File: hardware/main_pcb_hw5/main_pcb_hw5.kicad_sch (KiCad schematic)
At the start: 24 parts, among them J1 MEGA TOP, J10 GBA_Slot, J2 MEGA BOTTOM, J3 CART SLOT TOP ROW, J4 CART SLOT BOTTOM ROW, J5 MEGA SIDE, J6 5V USB, J7 Conn_01x07, J8 EXP2, J9 EXP1, M2_1 Screw_Terminal_01x01, M2_2 Screw_Terminal_01x01, M2_3 Screw_Terminal_01x01, M2_4 Screw_Terminal_01x01, M2_5 Screw_Terminal_01x01, M2_6 Screw_Terminal_01x01, M2_7 Screw_Terminal_01x01, M2_8 Screw_Terminal_01x01, M2_9 Screw_Terminal_01x01, SW1 VOLTAGE SWITCH, SW2 POWER SWITCH

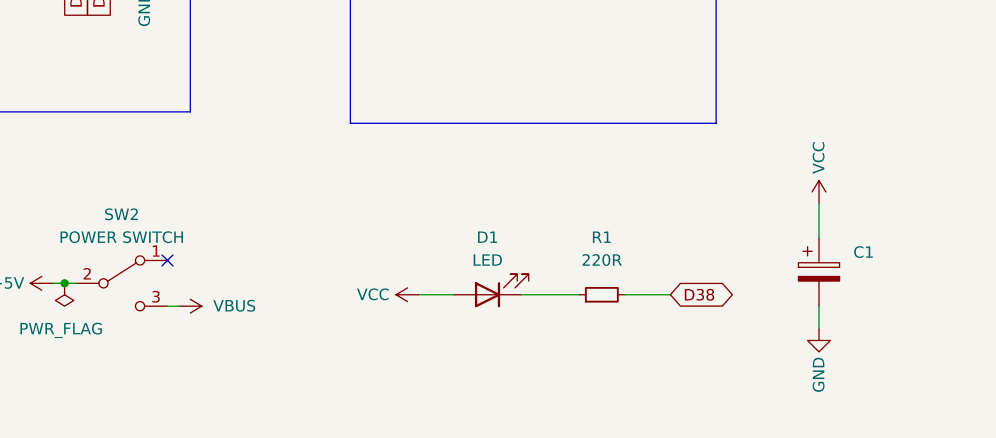
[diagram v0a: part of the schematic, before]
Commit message: Move switches to right side
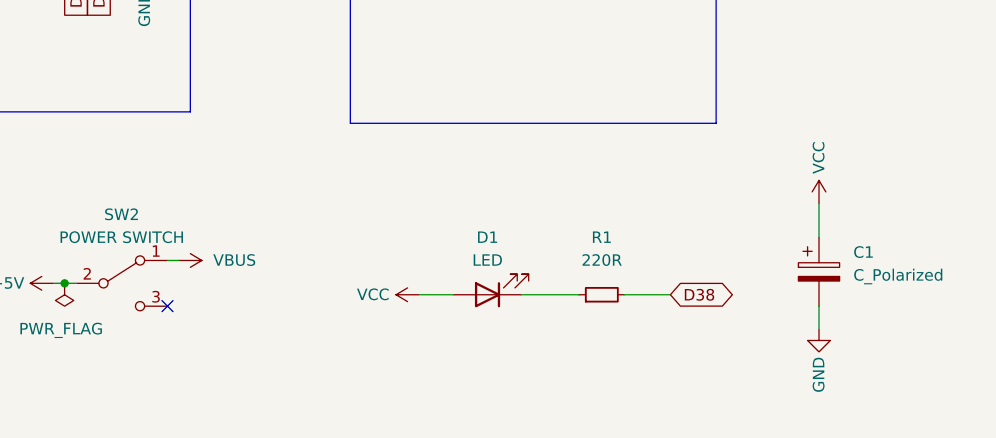
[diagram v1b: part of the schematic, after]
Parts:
- C1: value (none) -> C_Polarized
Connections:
- net VBUS: now also SW2.1 (A); no longer SW2.3 (C)
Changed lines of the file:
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@@
   (title_block
     (title "OSCR HW5")
-    (date "2022-05-16")
-    (rev "V1")
+    (date "2022-06-04")
+    (rev "V2")
   )
   (junction (at 248.92 45.72) (diameter 0) (color 0 0 0 0)
@@
   (no_connect (at 194.31 113.03))
   (no_connect (at 36.83 30.48))
-  (no_connect (at 199.39 149.86))
+  (no_connect (at 199.39 154.94))
   (no_connect (at 39.37 30.48))
   (no_connect (at 35.56 96.52))
@@
     (stroke (width 0) (type default) (color 0 0 0 0))
   )
-  (wire (pts (xy 199.39 154.94) (xy 200.66 154.94))
+  (wire (pts (xy 199.39 149.86) (xy 200.66 149.86))
     (stroke (width 0) (type default) (color 0 0 0 0))
   )
@@
     (pin "9")
   )
-  (symbol (lib_id "power:VBUS") (at 200.66 154.94 270) (unit 1)
+  (symbol (lib_id "power:VBUS") (at 200.66 149.86 270) (unit 1)
     (in_bom yes) (on_board yes) (fields_autoplaced)
-    (property "Reference" "#PWR0103" (id 0) (at 196.85 154.94 0)
-      (effects (font (size 1.27 1.27)) hide)
-    )
-    (property "Value" "VBUS" (id 1) (at 204.47 154.9399 90)
+    (property "Reference" "#PWR0103" (id 0) (at 196.85 149.86 0)
+      (effects (font (size 1.27 1.27)) hide)
+    )
+    (property "Value" "VBUS" (id 1) (at 204.47 149.8599 90)
       (effects (font (size 1.27 1.27)) (justify left))
     )
-    (property "Footprint" "" (id 2) (at 200.66 154.94 0)
-      (effects (font (size 1.27 1.27)) hide)
-    )
-    (property "Datasheet" "" (id 3) (at 200.66 154.94 0)
+    (property "Footprint" "" (id 2) (at 200.66 149.86 0)
+      (effects (font (size 1.27 1.27)) hide)
+    )
+    (property "Datasheet" "" (id 3) (at 200.66 149.86 0)
       (effects (font (size 1.27 1.27)) hide)
     )
@@
       (effects (font (size 1.27 1.27)) (justify left))
     )
-    (property "Value" "" (id 1) (at 275.59 151.5109 0)
+    (property "Value" "C_Polarized" (id 1) (at 275.59 151.5109 0)
       (effects (font (size 1.27 1.27)) (justify left))
     )

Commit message: Add HW5 Rev. 3
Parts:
- added JP1: Arduino powered by VCC, symbol Jumper:SolderJumper_2_Open
- added JP2: Arduino powered by 5V, symbol Jumper:SolderJumper_2_Open
- added JP3: (no value), symbol Jumper:SolderJumper_2_Open
- SW1: value VOLTAGE SWITCH -> (none)
- SW2: value POWER SWITCH -> (none)
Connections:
- net +3V3: now also JP3.2 (B)
- net +5V: now also JP2.1 (A)
- net VCC: now also JP1.1 (A); no longer J1.37 (Pin_37), J1.38 (Pin_38)
- net +3.3VA: now reaches J1.35 (Pin_35)
- net +3.3VA: now also J1.36 (Pin_36), JP3.1 (A)
- new net VDDA: J1.37 (Pin_37), J1.38 (Pin_38), JP1.2 (B), JP2.2 (B)
- no-connect marks 12 -> 10

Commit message: Update silkscreen
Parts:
- JP1: value Arduino powered by VCC -> (none)
- JP2: value Arduino powered by 5V -> (none)
- SW1: value (none) -> VOLTAGE
- SW2: value (none) -> POWER
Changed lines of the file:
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@@
     (in_bom yes) (on_board yes) (fields_autoplaced)
     (property "Reference" "JP2" (id 0) (at 31.75 182.88 0))
-    (property "Value" "Arduino powered by 5V" (id 1) (at 31.75 185.42 0))
+    (property "Value" "" (id 1) (at 31.75 185.42 0))
     (property "Footprint" "" (id 2) (at 31.75 189.23 0)
       (effects (font (size 1.27 1.27)) hide)
@@
     (in_bom yes) (on_board yes) (fields_autoplaced)
     (property "Reference" "JP1" (id 0) (at 31.75 171.45 0))
-    (property "Value" "Arduino powered by VCC" (id 1) (at 31.75 173.99 0))
+    (property "Value" "" (id 1) (at 31.75 173.99 0))
     (property "Footprint" "" (id 2) (at 31.75 177.8 0)
       (effects (font (size 1.27 1.27)) hide)
@@
     (in_bom yes) (on_board yes) (fields_autoplaced)
     (property "Reference" "SW2" (id 0) (at 194.31 144.78 0))
-    (property "Value" "" (id 1) (at 194.31 147.32 0))
+    (property "Value" "POWER" (id 1) (at 194.31 147.32 0))
     (property "Footprint" "" (id 2) (at 194.31 152.4 0)
       (effects (font (size 1.27 1.27)) hide)
@@
       (effects (font (size 1.27 1.27)) hide)
     )
-    (property "Value" "" (id 1) (at 43.18 86.36 90))
+    (property "Value" "+3.3VA" (id 1) (at 43.18 86.36 90))
     (property "Footprint" "" (id 2) (at 43.18 92.71 0)
       (effects (font (size 1.27 1.27)) hide)
@@
     (in_bom yes) (on_board yes) (fields_autoplaced)
     (property "Reference" "SW1" (id 0) (at 161.29 144.78 0))
-    (property "Value" "" (id 1) (at 161.29 147.32 0))
+    (property "Value" "VOLTAGE" (id 1) (at 161.29 147.32 0))
     (property "Footprint" "" (id 2) (at 161.29 152.4 0)
       (effects (font (size 1.27 1.27)) hide)
@@
     )
     (path "/9b821643-0a09-4ed0-af40-76467a90d5d5"
-      (reference "JP1") (unit 1) (value "Arduino powered by VCC") (footprint "")
+      (reference "JP1") (unit 1) (value "J1") (footprint "")
     )
     (path "/5b67058f-fbd0-4ef7-ae7b-c94a6074918c"
-      (reference "JP2") (unit 1) (value "Arduino powered by 5V") (footprint "")
+      (reference "JP2") (unit 1) (value "Testpoints 1 2") (footprint "")
     )
     (path "/370f34de-8b3d-462d-a13b-4bf97a89f644"
-      (reference "JP3") (unit 1) (value "3V3 from Arduino") (footprint "")
+      (reference "JP3") (unit 1) (value "Testpoints 3 4") (footprint "")
     )
     (path "/faa5946b-601d-4ca8-bb98-7d46d4f7daf3"

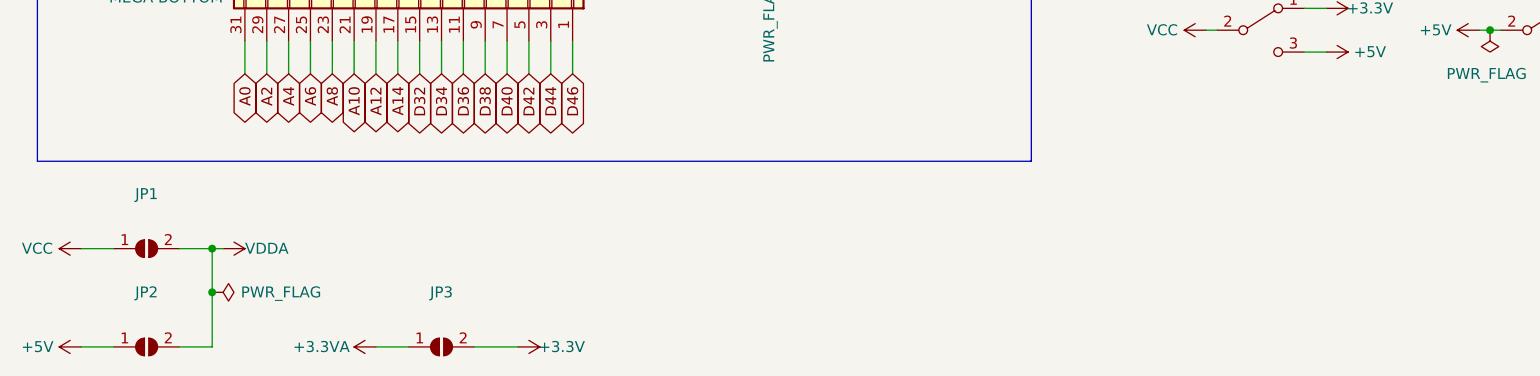
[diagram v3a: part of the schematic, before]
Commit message: New OSCR Logo + Vselect built into main PCB
Also added symbol and footprint library links
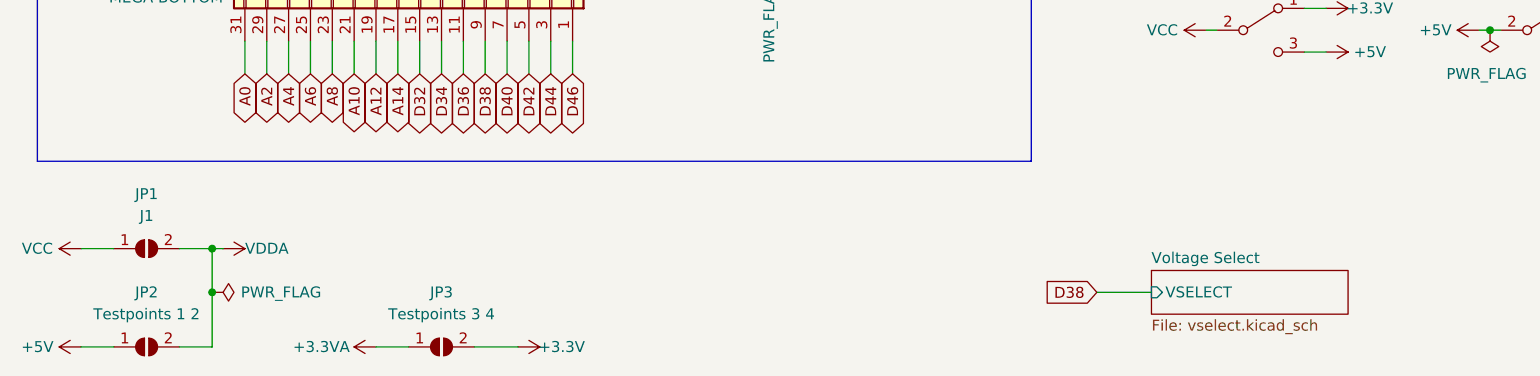
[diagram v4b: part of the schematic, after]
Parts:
- JP1: value (none) -> J1
- JP2: value (none) -> Testpoints 1 2
- JP3: value (none) -> Testpoints 3 4
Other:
- added sheet Voltage Select (vselect.kicad_sch)
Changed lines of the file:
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@@
     (title "OSCR HW5")
     (date "2022-06-19")
-    (rev "V3")
+    (rev "V4")
   )
   (junction (at 248.92 45.72) (diameter 0) (color 0 0 0 0)
@@
     (stroke (width 0) (type default) (color 0 0 0 0))
   )
+  (wire (pts (xy 142.24 182.88) (xy 148.59 182.88))
+    (stroke (width 0) (type default) (color 0 0 0 0))
+  )
   (wire (pts (xy 43.18 92.71) (xy 43.18 96.52))
     (stroke (width 0) (type default) (color 0 0 0 0))
@@
     )
   )
+  (global_label "D38" (shape input) (at 142.24 182.88 180) (fields_autoplaced)
+    (effects (font (size 1.27 1.27)) (justify right))
+    (property "Intersheet References" "${INTERSHEET_REFS}" (id 0) (at 136.1379 182.8006 0)
+      (effects (font (size 1.27 1.27)) (justify right) hide)
+    )
+  )
   (global_label "A9" (shape bidirectional) (at 64.77 34.29 270) (fields_autoplaced)
     (effects (font (size 1.27 1.27)) (justify right))
@@
     (in_bom yes) (on_board yes) (fields_autoplaced)
     (property "Reference" "JP3" (id 0) (at 66.04 182.88 0))
-    (property "Value" "" (id 1) (at 66.04 185.42 0))
+    (property "Value" "Testpoints 3 4" (id 1) (at 66.04 185.42 0))
     (property "Footprint" "" (id 2) (at 66.04 189.23 0)
       (effects (font (size 1.27 1.27)) hide)
@@
     (in_bom yes) (on_board yes) (fields_autoplaced)
     (property "Reference" "JP2" (id 0) (at 31.75 182.88 0))
-    (property "Value" "" (id 1) (at 31.75 185.42 0))
+    (property "Value" "Testpoints 1 2" (id 1) (at 31.75 185.42 0))
     (property "Footprint" "" (id 2) (at 31.75 189.23 0)
       (effects (font (size 1.27 1.27)) hide)
@@
     (in_bom yes) (on_board yes) (fields_autoplaced)
     (property "Reference" "JP1" (id 0) (at 31.75 171.45 0))
-    (property "Value" "" (id 1) (at 31.75 173.99 0))
+    (property "Value" "J1" (id 1) (at 31.75 173.99 0))
     (property "Footprint" "" (id 2) (at 31.75 177.8 0)
       (effects (font (size 1.27 1.27)) hide)
@@
     (pin "1")
   )
+  (sheet (at 148.59 180.34) (size 22.86 5.08) (fields_autoplaced)
+    (stroke (width 0.1524) (type solid) (color 0 0 0 0))
+    (fill (color 0 0 0 0.0000))
+    (property "Sheet name" "Voltage Select" (id 0) (at 148.59 179.6284 0)
+      (effects (font (size 1.27 1.27)) (justify left bottom))
+    )
+    (property "Sheet file" "vselect.kicad_sch" (id 1) (at 148.59 186.0046 0)
+      (effects (font (size 1.27 1.27)) (justify left top))
+    )
+    (pin "VSELECT" input (at 148.59 182.88 180)
+      (effects (font (size 1.27 1.27)) (justify left))
+    )
+  )
   (sheet_instances
     (path "/" (page "1"))
+    (path "/4688c134-9ce3-46e1-b4dc-a534603502d3" (page "2"))
   )
   (symbol_instances
@@
       (reference "#PWR06") (unit 1) (value "GND") (footprint "")
     )
+    (path "/4688c134-9ce3-46e1-b4dc-a534603502d3/5c397657-1146-4b70-bb5d-229224395044"
+      (reference "#PWR07") (unit 1) (value "+3V3") (footprint "")
+    )
+    (path "/4688c134-9ce3-46e1-b4dc-a534603502d3/945f52f0-4060-41a7-9172-d7319cb2423e"
+      (reference "#PWR08") (unit 1) (value "+5V") (footprint "")
+    )
     (path "/ba6a2da9-e81c-4153-8ffb-600cd4b388a1"
       (reference "#PWR09") (unit 1) (value "VBUS") (footprint "")
@@
       (reference "#PWR015") (unit 1) (value "+3.3V") (footprint "")
     )
+    (path "/4688c134-9ce3-46e1-b4dc-a534603502d3/cb3714fe-1058-4a1c-8847-50cfc7804385"
+      (reference "#PWR016") (unit 1) (value "GND") (footprint "")
+    )
     (path "/3260f30c-1ad1-4e0b-ad50-51792b0195b1"
       (reference "#PWR017") (unit 1) (value "VCC") (footprint "")
@@
       (reference "#PWR021") (unit 1) (value "+5V") (footprint "")
     )
+    (path "/4688c134-9ce3-46e1-b4dc-a534603502d3/dfe5754d-9985-4214-a749-5e6b6ce0b04a"
+      (reference "#PWR022") (unit 1) (value "VCC") (footprint "")
+    )
     (path "/018152fb-a659-4d33-bed2-870e6138ecbc"
       (reference "#PWR024") (unit 1) (value "VCC") (footprint "")
@@
       (reference "C1") (unit 1) (value "C_Polarized") (footprint "")
     )
+    (path "/4688c134-9ce3-46e1-b4dc-a534603502d3/a87f794b-d2c9-48ec-9dfa-57253999f610"
+      (reference "C2") (unit 1) (value "0.1 uF") (footprint "Capacitor_SMD:C_0402_1005Metric_Pad0.74x0.62mm_HandSolder")
+    )
+    (path "/4688c134-9ce3-46e1-b4dc-a534603502d3/a4d66296-f69c-4e34-ae3d-ecf61737aa5b"
+      (reference "C3") (unit 1) (value "0.1 uF") (footprint "Capacitor_SMD:C_0402_1005Metric_Pad0.74x0.62mm_HandSolder")
+    )
+    (path "/4688c134-9ce3-46e1-b4dc-a534603502d3/19b1de5c-7eb5-4e2b-ba2c-4a931aab2613"
+      (reference "C4") (unit 1) (value "10 uF") (footprint "Capacitor_SMD:C_0402_1005Metric_Pad0.74x0.62mm_HandSolder")
+    )
     (path "/e45b3f20-40e6-4c90-8100-685db63993ad"
       (reference "D1") (unit 1) (value "LED") (footprint "")
@@
       (reference "R1") (unit 1) (value "220R") (footprint "")
     )
+    (path "/4688c134-9ce3-46e1-b4dc-a534603502d3/df77b9b1-4924-4151-8eac-93b44113b4e8"
+      (reference "R2") (unit 1) (value "550") (footprint "Resistor_SMD:R_0402_1005Metric_Pad0.72x0.64mm_HandSolder")
+    )
     (path "/dd184fc1-799a-4fa0-88eb-e4a59cd75459"
       (reference "SW1") (unit 1) (value "VOLTAGE") (footprint "")
@@
       (reference "SW2") (unit 1) (value "POWER") (footprint "")
     )
+    (path "/4688c134-9ce3-46e1-b4dc-a534603502d3/8d4abe18-0a15-4edc-8fa8-449f59f0f043"
+      (reference "U1") (unit 1) (value "TPS2113PW") (footprint "Personal:Texas_Instruments-TPS2113PW-Level_A")
+    )
   )
